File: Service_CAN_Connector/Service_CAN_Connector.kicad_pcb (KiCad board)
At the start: 2 copper layers, 100 x 99.4 mm, 173 parts, among them J1 CAN1, J10 Shield, J11 Shield, J12 Shield, J13 CAN Power, J14 CAN1_Terminator, J15 CAN1_Terminator, J16 CAN1_Terminator, J17 CAN1_Terminator, J18 CAN1_Terminator, J19 GND, J2 CAN2, J20 GND, J21 12V, J22 12V, J23 GND, J24 GND, J25 12V, J26 12V, J27 GND, J28 GND, J29 12V, J3 CAN3, J30 12V, J31 GND, J32 GND, J33 12V, J34 12V, J4 CAN4, J5 Molex 10pin, J6 CAN5, J7 CAN Power, J8 Shield, J9 Shield

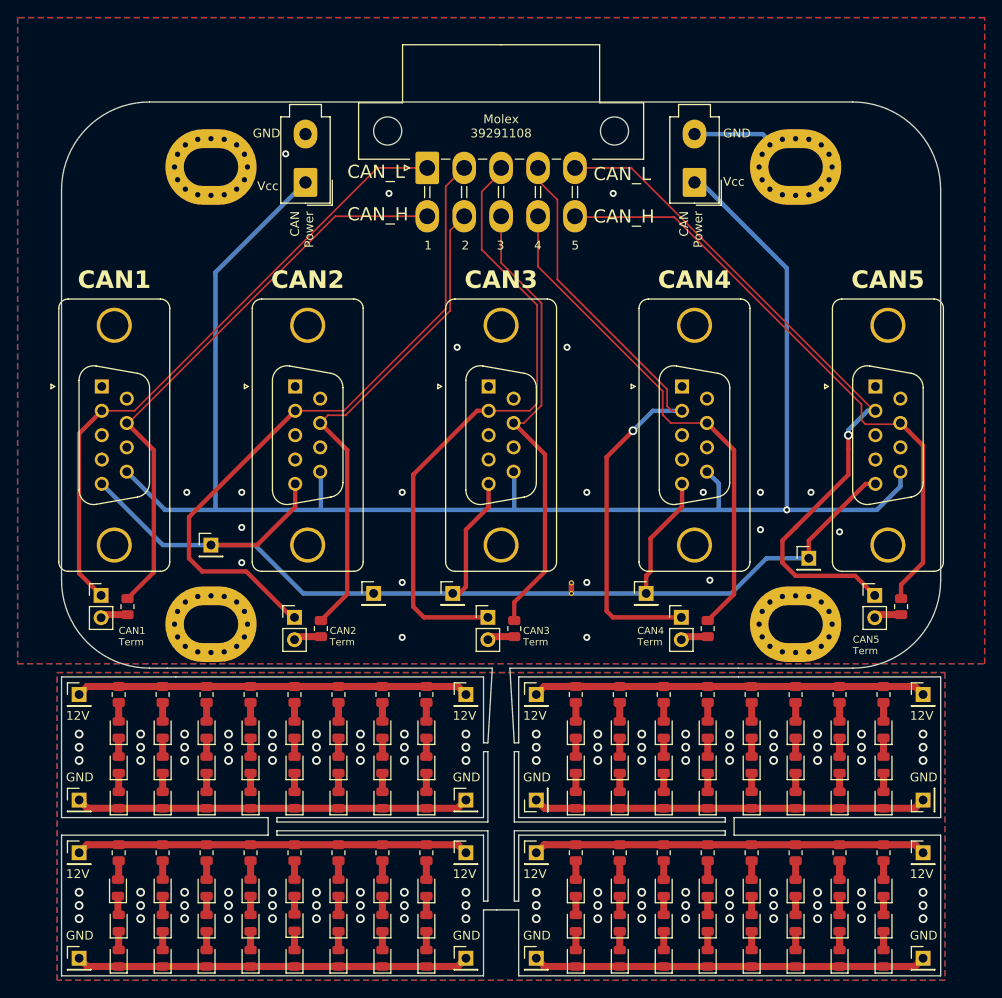
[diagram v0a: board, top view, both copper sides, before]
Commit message: Service can connector Rev B
Also added molex 10 pin connector 3d model
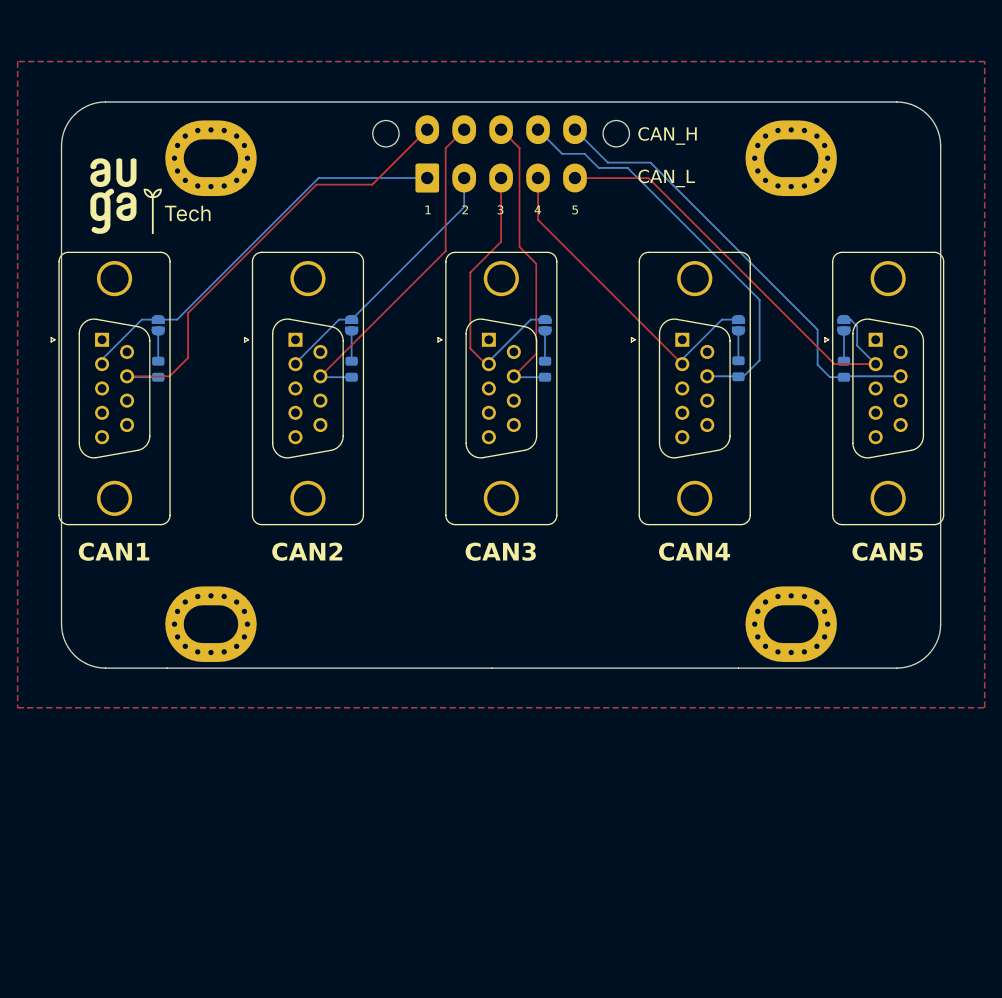
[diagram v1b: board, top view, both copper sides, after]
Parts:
- removed D1, D10, D11, D12, D13, D14, D15, D16, D17, D18, D19, D2, D20, D21, D22, D23, D24, D25, D26, D27, D28, D29, D3, D30, D31, D32, D33, D34, D35, D36, D37, D38, D39, D4, D40, D41, D42, D43, D44, D45, D46, D47, D48, D49, D5, D50, D51, D52, D53, D54, D55, D56, D57, D58, D59, D6, D60, D61, D62, D63, D64, D65, D66, D67, D68, D69, D7, D70, D71, D72, D73, D74, D75, D76, D77, D78, D79, D8, D80, D81, D82, D83, D84, D85, D86, D87, D88, D89, D9, D90, D91, D92, D93, D94, D95, D96: LED, LED_SMD:LED_0805_2012Metric
- removed J10, J11, J12, J8, J9: Shield, Connector_PinHeader_2.54mm:PinHeader_1x01_P2.54mm_Vertical
- removed J13, J7: CAN Power, Connector_Molex:Molex_Mini-Fit_Jr_5566-02A_2x01_P4.20mm_Vertical
- removed J14, J15, J16, J17, J18: CAN1_Terminator, Connector_PinHeader_2.54mm:PinHeader_1x02_P2.54mm_Vertical
- removed J19, J20, J23, J24, J27, J28, J31, J32: GND, Connector_PinHeader_2.54mm:PinHeader_1x01_P2.54mm_Vertical
- removed J21, J22, J25, J26, J29, J30, J33, J34: 12V, Connector_PinHeader_2.54mm:PinHeader_1x01_P2.54mm_Vertical
- removed NT1: NetTie_2, NetTie:NetTie-2_THT_Pad0.3mm
- removed R10, R11, R12, R13, R14, R15, R16, R17, R18, R19, R20, R21, R22, R23, R24, R25, R26, R27, R28, R29, R30, R31, R32, R33, R34, R35, R36, R37, R4, R5, R8, R9: 120 Ohm, Resistor_SMD:R_0805_2012Metric
- added JP1: CAN1_Terminator, Jumper:SolderJumper-2_P1.3mm_Open_RoundedPad1.0x1.5mm, B.Cu at (76.0, 60.0)
- added JP2: CAN2_Terminator, Jumper:SolderJumper-2_P1.3mm_Open_RoundedPad1.0x1.5mm, B.Cu at (98.0, 60.0)
- added JP3: CAN3_Terminator, Jumper:SolderJumper-2_P1.3mm_Open_RoundedPad1.0x1.5mm, B.Cu at (120.0, 60.0)
- added JP4: CAN4_Terminator, Jumper:SolderJumper-2_P1.3mm_Open_RoundedPad1.0x1.5mm, B.Cu at (142.0, 60.0)
- added JP5: CAN5_Terminator, Jumper:SolderJumper-2_P1.3mm_Open_RoundedPad1.0x1.5mm, B.Cu at (154.0, 60.0)
- G1: moved to F.Cu
- J5: footprint Connector_Molex:Molex_Mini-Fit_Jr_5569-10A1_2x05_P4.20mm_Horizontal -> Connector_Molex:Molex_Mini-Fit_Jr_5566-10A2_2x05_P4.20mm_Vertical; moved to B.Cu
- R1, R2, R3, R6, R7: moved to B.Cu
- moved R7 57.1 mm to (120.0, 65.0), turned to -90 degrees
- moved R1 55.9 mm to (142.0, 65.0), turned to -90 degrees
- moved R3 47.7 mm to (154.0, 65.0), turned to -90 degrees
- moved R6 45.5 mm to (98.0, 65.0), turned to -90 degrees
- moved R2 27.2 mm to (76.0, 65.0), turned to -90 degrees
- moved G1 6.79 mm to (75.1, 45.3), turned to 0 degrees
- moved J1 5.31 mm to (69.6, 61.6)
- moved J2 5.31 mm to (91.6, 61.6)
- moved J3 5.31 mm to (113.6, 61.6)
- moved J4 5.31 mm to (135.6, 61.6)
- moved J6 5.31 mm to (157.6, 61.6)
- moved J5 1.15 mm to (106.6, 43.2)
- moved H3 1.12 mm to (148.0, 41.0)
- moved H2 1.00 mm to (82.0, 41.0)
- moved H4 0.50 mm to (148.0, 94.0)
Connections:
- J1 pad 5: Shield -> unconnected-(J1-Pad5)
- J1 pad 9: VCC -> unconnected-(J1-Pad9)
- J2 pad 5: Shield -> unconnected-(J2-Pad5)
- J2 pad 9: VCC -> unconnected-(J2-Pad9)
- J3 pad 5: Shield -> unconnected-(J3-Pad5)
- J3 pad 9: VCC -> unconnected-(J3-Pad9)
- J4 pad 5: Shield -> unconnected-(J4-Pad5)
- J4 pad 9: VCC -> unconnected-(J4-Pad9)
- J6 pad 5: Shield -> unconnected-(J6-Pad5)
- J6 pad 9: VCC -> unconnected-(J6-Pad9)
- R1 pad 2: /CAN2+ -> /CAN4+
- R3 pad 2: /CAN3+ -> /CAN5+
- R6 pad 2: +12V -> /CAN2+
- R7 pad 2: +12V -> /CAN3+
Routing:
- net VCC: track 189.8 -> 0.00 mm, vias 1 -> 0
- net GNDA: track 179.1 -> 0.00 mm, vias 108 -> 0
- net +12V: track 179.0 -> 0.00 mm
- net Shield: track 142.2 -> 0.00 mm
- net /CAN2-: track 75.4 -> 30.0 mm
- net /CAN3-: track 71.8 -> 32.4 mm
- net /CAN4-: track 72.6 -> 36.8 mm, vias 1 -> 0
- net /CAN5-: track 79.9 -> 50.0 mm, vias 1 -> 0
- net /CAN1-: track 71.6 -> 46.1 mm
- net /CAN5+: track 70.0 -> 51.1 mm
- net /CAN3+: track 52.8 -> 34.4 mm
- net /CAN2+: track 56.5 -> 38.4 mm
- net /CAN1+: track 66.4 -> 52.4 mm
- net GND: track 13.1 -> 0.00 mm, vias 21 -> 0
- net /CAN4+: track 58.9 -> 46.9 mm
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- removed copper zone on B.Cu, net GNDA
- removed copper zone on F.Cu, net GNDA
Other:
- board size 100 x 99.4 mm -> 100 x 64.4 mm
- board text added: "6"
- board text added: "9"
- board text added: "CAN1 120 Terminator"
- board text added: "CAN2 120 Terminator"
- board text added: "CAN3 120 Terminator"
- board text added: "CAN4 120 Terminator"
- board text added: "CAN5 120 Terminator"
- board text added: "CAN_H CAN_L"
- board text added: "D. Vaitiekus 2024-08-29 Service CAN Splitter Rev B AUGA Tech"
- board text added: "H"
- board text added: "L"
- board text added: "Molex 39299103"
- board text removed: "12V"
- board text removed: "CAN Power"
- board text removed: "CAN1 Term"
- board text removed: "CAN2 Term"
- board text removed: "CAN3 Term"
- board text removed: "CAN4 Term"
- board text removed: "CAN5 Term"
- board text removed: "CAN_L CAN_H"
- board text removed: "D. Vaitiekus 2024-06-28 Service CAN Splitter Rev A AUGA Tech"
- board text removed: "GND"
- board text removed: "Molex 39291108"
- board text removed: "Vcc"
